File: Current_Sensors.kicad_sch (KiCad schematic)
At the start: 12 parts

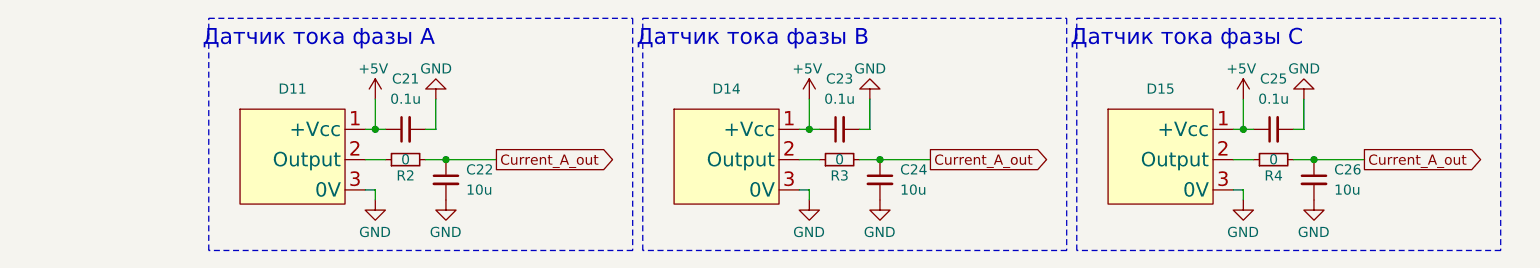
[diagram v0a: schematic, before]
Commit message: Добавил температурные контуры звщиты
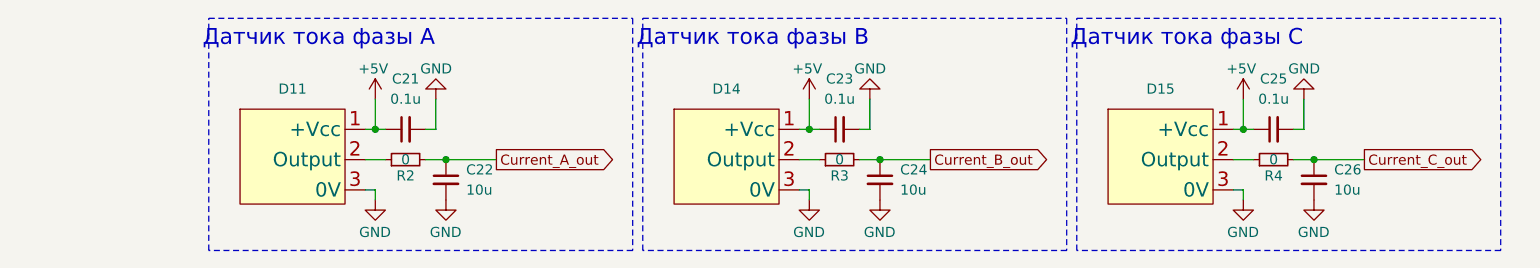
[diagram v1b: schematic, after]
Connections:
- net Current_A_out: no longer C24.1, C26.1, R3.2, R4.2
- new net Current_B_out: C24.1, R3.2
- new net Current_C_out: C26.1, R4.2
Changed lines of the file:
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@@
 		)
 	)
-	(global_label "Current_A_out"
+	(global_label "Current_B_out"
 		(shape output)
 		(at 162.56 109.22 0)
@@
 		)
 		(property "Intersheetrefs" "${INTERSHEET_REFS}"
-			(at 177.1447 109.22 0)
+			(at 177.0181 109.22 0)
 			(effects
 				(font
@@
 		)
 	)
-	(global_label "Current_A_out"
+	(global_label "Current_C_out"
 		(shape output)
 		(at 217.17 109.22 0)
@@
 		)
 		(property "Intersheetrefs" "${INTERSHEET_REFS}"
-			(at 231.7547 109.22 0)
+			(at 231.5003 109.22 0)
 			(effects
 				(font

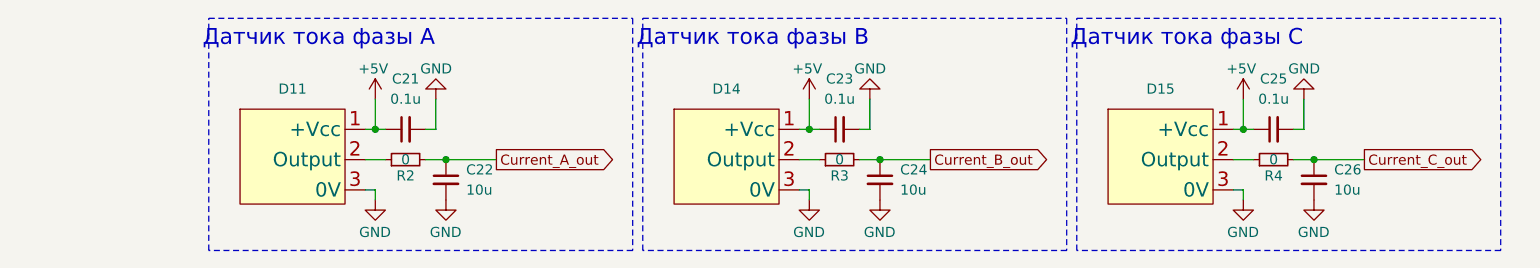
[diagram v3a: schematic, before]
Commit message: Исправления: исправил нумерацию ножек датчиков тока
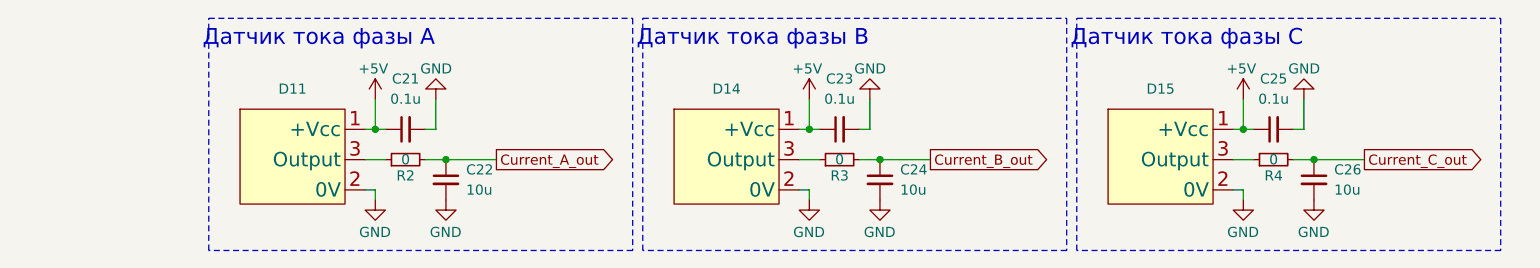
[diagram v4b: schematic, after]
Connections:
- net GND: now also D11.2 (0V), D14.2 (0V), D15.2 (0V); no longer D11.3 (0V), D14.3 (0V), D15.3 (0V)
- net at R2.1: now also D11.3 (Output); no longer D11.2 (Output)
- net at R4.1: now also D15.3 (Output); no longer D15.2 (Output)
- net at R3.1: now also D14.3 (Output); no longer D14.2 (Output)
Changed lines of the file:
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@@
 	)
 	(symbol
-		(lib_name "GND_8")
 		(lib_id "power:GND")
 		(at 209.55 101.6 180)
@@
 			)
 		)
-		(property "Description" ""
+		(property "Description" "Power symbol creates a global label with name \"GND\" , ground"
 			(at 209.55 101.6 0)
 			(effects
@@
 			)
 		)
-		(property "Description" ""
+		(property "Description" "Power symbol creates a global label with name \"GND\" , ground"
 			(at 201.93 114.3 0)
 			(effects
@@
 	)
 	(symbol
-		(lib_name "GND_7")
 		(lib_id "power:GND")
 		(at 210.82 114.3 0)
@@
 			)
 		)
-		(property "Description" ""
+		(property "Description" "Power symbol creates a global label with name \"GND\" , ground"
 			(at 210.82 114.3 0)
 			(effects
@@
 	)
 	(symbol
-		(lib_name "GND_3")
 		(lib_id "power:GND")
 		(at 100.33 101.6 180)
@@
 			)
 		)
-		(property "Description" ""
+		(property "Description" "Power symbol creates a global label with name \"GND\" , ground"
 			(at 100.33 101.6 0)
 			(effects
@@
 	)
 	(symbol
-		(lib_name "GND_2")
 		(lib_id "power:GND")
 		(at 154.94 101.6 180)
@@
 			)
 		)
-		(property "Description" ""
+		(property "Description" "Power symbol creates a global label with name \"GND\" , ground"
 			(at 154.94 101.6 0)
 			(effects
@@
 	)
 	(symbol
-		(lib_name "GND_6")
 		(lib_id "power:GND")
 		(at 92.71 114.3 0)
@@
 			)
 		)
-		(property "Description" ""
+		(property "Description" "Power symbol creates a global label with name \"GND\" , ground"
 			(at 92.71 114.3 0)
 			(effects
@@
 	)
 	(symbol
-		(lib_name "GND_1")
 		(lib_id "power:GND")
 		(at 101.6 114.3 0)
@@
 			)
 		)
-		(property "Description" ""
+		(property "Description" "Power symbol creates a global label with name \"GND\" , ground"
 			(at 101.6 114.3 0)
 			(effects
@@
 	)
 	(symbol
-		(lib_name "GND_4")
 		(lib_id "power:GND")
 		(at 156.21 114.3 0)
@@
 			)
 		)
-		(property "Description" ""
+		(property "Description" "Power symbol creates a global label with name \"GND\" , ground"
 			(at 156.21 114.3 0)
 			(effects
@@
 	)
 	(symbol
-		(lib_name "GND_5")
 		(lib_id "power:GND")
 		(at 147.32 114.3 0)
@@
 			)
 		)
-		(property "Description" ""
+		(property "Description" "Power symbol creates a global label with name \"GND\" , ground"
 			(at 147.32 114.3 0)
 			(effects

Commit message: VER2.0: отпаравил файлы в китай, обновил BOM
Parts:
- D11, D14, D15: value ~ -> YMC15S-1000A
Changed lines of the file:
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@@
 	(text "Датчик тока фазы C"
 		(exclude_from_sim no)
-		(at 194.818 93.98 0)
+		(at 197.485 93.98 0)
 		(effects
 			(font
@@
 	(text "Датчик тока фазы B"
 		(exclude_from_sim no)
-		(at 140.208 93.98 0)
+		(at 142.875 93.98 0)
 		(effects
 			(font
@@
 	(text "Датчик тока фазы А"
 		(exclude_from_sim no)
-		(at 85.598 93.98 0)
+		(at 88.265 93.98 0)
 		(effects
 			(font
@@
 		(on_board yes)
 		(dnp no)
-		(fields_autoplaced yes)
 		(property "Reference" "D11"
-			(at 82.296 100.33 0)
-			(effects
-				(font
-					(size 1.27 1.27)
-				)
-			)
-		)
-		(property "Value" "~"
+			(at 82.55 99.695 0)
+			(effects
+				(font
+					(size 1.27 1.27)
+				)
+			)
+		)
+		(property "Value" "YMC15S-1000A"
 			(at 82.296 101.6 0)
 			(effects
@@
 			)
 		)
-		(property "Description" "YMC15S-500A"
+		(property "Description" "YMC15S-1000A"
 			(at 82.55 102.87 0)
 			(effects
@@
 		(on_board yes)
 		(dnp no)
-		(fields_autoplaced yes)
 		(property "Reference" "D14"
-			(at 136.906 100.33 0)
-			(effects
-				(font
-					(size 1.27 1.27)
-				)
-			)
-		)
-		(property "Value" "~"
+			(at 137.16 99.695 0)
+			(effects
+				(font
+					(size 1.27 1.27)
+				)
+			)
+		)
+		(property "Value" "YMC15S-1000A"
 			(at 136.906 101.6 0)
 			(effects
@@
 			)
 		)
-		(property "Description" "YMC15S-500A"
+		(property "Description" "YMC15S-1000A"
 			(at 137.16 102.87 0)
 			(effects
@@
 		(on_board yes)
 		(dnp no)
-		(fields_autoplaced yes)
 		(property "Reference" "D15"
-			(at 191.516 100.33 0)
-			(effects
-				(font
-					(size 1.27 1.27)
-				)
-			)
-		)
-		(property "Value" "~"
+			(at 191.77 99.695 0)
+			(effects
+				(font
+					(size 1.27 1.27)
+				)
+			)
+		)
+		(property "Value" "YMC15S-1000A"
 			(at 191.516 101.6 0)
 			(effects
@@
 			)
 		)
-		(property "Description" "YMC15S-500A"
+		(property "Description" "YMC15S-1000A"
 			(at 191.77 102.87 0)
 			(effects

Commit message: VER2.2: все изменения в списке изменений
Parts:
- D11, D14, D15: value YMC15S-1000A -> ~; Description P/N (none) -> Current sensor; Product Name (none) -> YMC15S-1000A

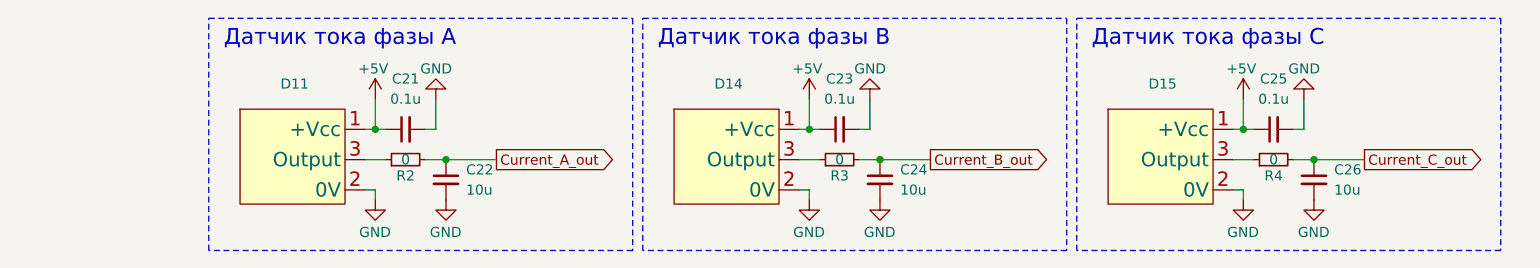
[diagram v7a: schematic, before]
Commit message: VER2.2: добавил фильтры на вход ШИМа и обновил все доки
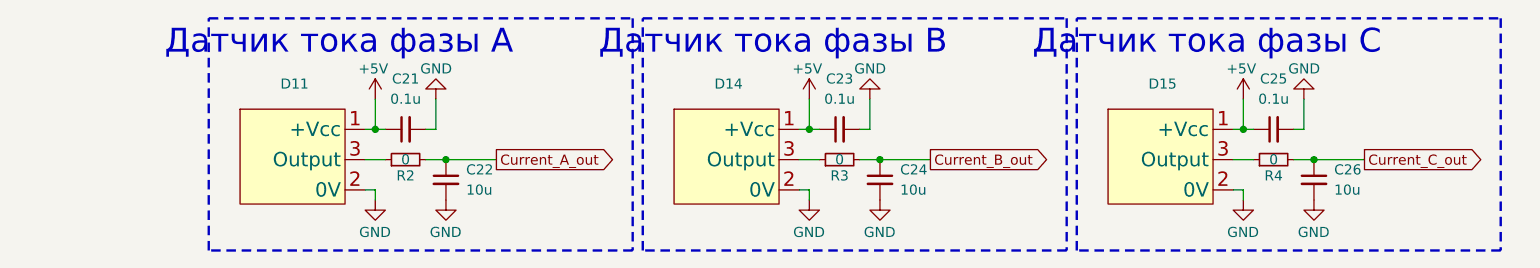
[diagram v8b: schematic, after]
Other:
- company: (none) -> ООО "ЭТТ"
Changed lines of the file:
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@@
 	(generator_version "9.0")
 	(paper "A4")
+	(title_block
+		(date "2025-06-04")
+		(company "ООО \"ЭТТ\"")
+	)
 	(rectangle
 		(start 71.755 91.44)
 		(end 125.095 120.65)
 		(stroke
-			(width 0)
+			(width 0.3)
 			(type dash)
 		)
@@
 		(end 179.705 120.65)
 		(stroke
-			(width 0)
+			(width 0.3)
 			(type dash)
 		)
@@
 		(end 234.315 120.65)
 		(stroke
-			(width 0)
+			(width 0.3)
 			(type dash)
 		)
@@
 	(text "Датчик тока фазы C"
 		(exclude_from_sim no)
-		(at 197.485 93.98 0)
+		(at 197.358 94.488 0)
 		(effects
 			(font
-				(size 2 2)
+				(size 3 3)
 			)
 		)
@@
 	(text "Датчик тока фазы B"
 		(exclude_from_sim no)
-		(at 142.875 93.98 0)
+		(at 142.748 94.488 0)
 		(effects
 			(font
-				(size 2 2)
+				(size 3 3)
 			)
 		)
@@
 	(text "Датчик тока фазы А"
 		(exclude_from_sim no)
-		(at 88.265 93.98 0)
+		(at 88.138 94.488 0)
 		(effects
 			(font
-				(size 2 2)
+				(size 3 3)
 			)
 		)
